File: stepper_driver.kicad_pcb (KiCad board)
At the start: 4 copper layers, 60 x 46 mm, 51 parts, among them IC1 TMC2590-TA-Trinamic, J1 BARREL_JACK, J2 Screw_Terminal_01x04, J3 CONN_01X14, J9 USB_C_Receptacle_USB2.0, Q1 Q_NPN_BEC, Q2 NCE4614, Q3 NCE4614, Q4 Q_NPN_BEC, Q5 NCE4614, Q6 NCE4614, SW1 SW_Push, U1 CH340G, U2 XC6210B332MR, U3 XL1509-5.0, U4 ESP32-WROOM-32, U6 SN74LV1T34DBV, Y1 12MHz

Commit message: Added PCB v1
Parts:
- C8: value 1uF/50V -> 1uF; footprint Capacitor_SMD:C_0603_1608Metric -> Capacitor_SMD:C_0402_1005Metric
- moved C8 0.81 mm to (138.2, 115.7)
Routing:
- net GND: track 148.5 -> 149.3 mm

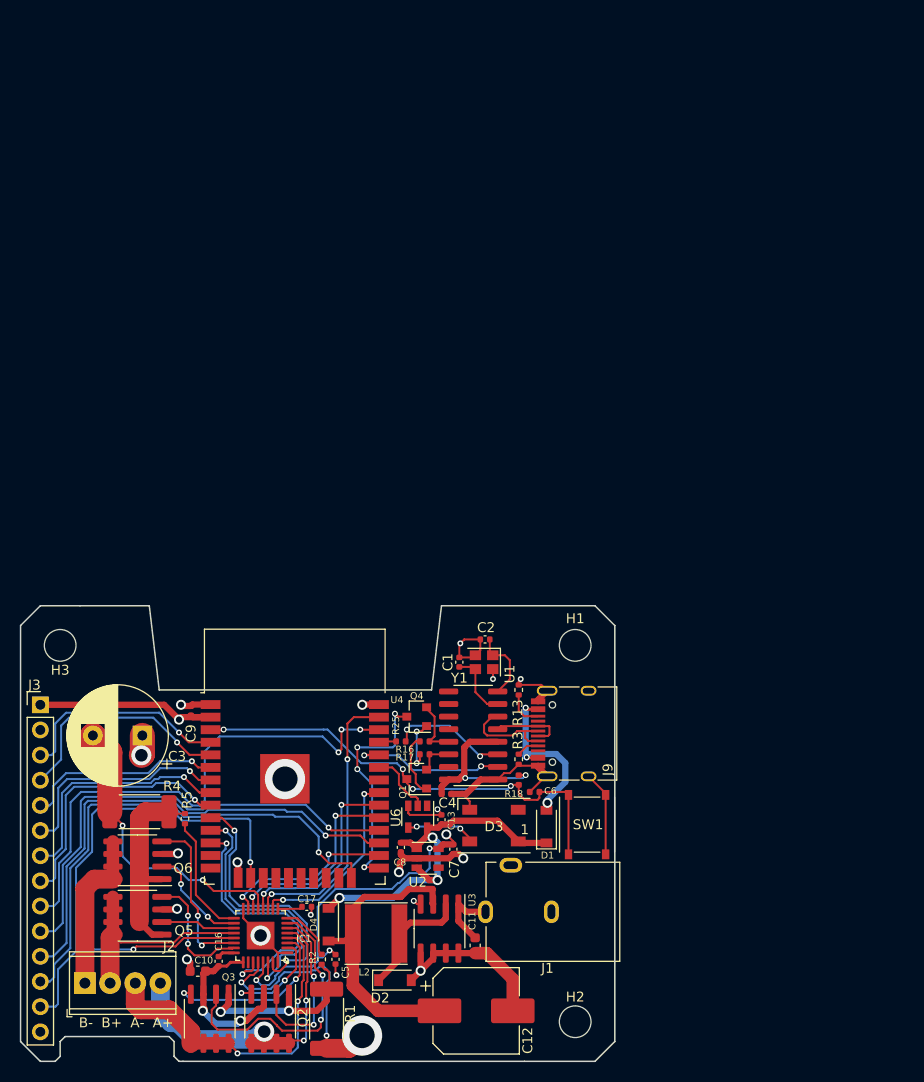
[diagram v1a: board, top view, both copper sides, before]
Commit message: Hardware design v2 with TMC2160 driver and NEMA 23 form factor for mounting
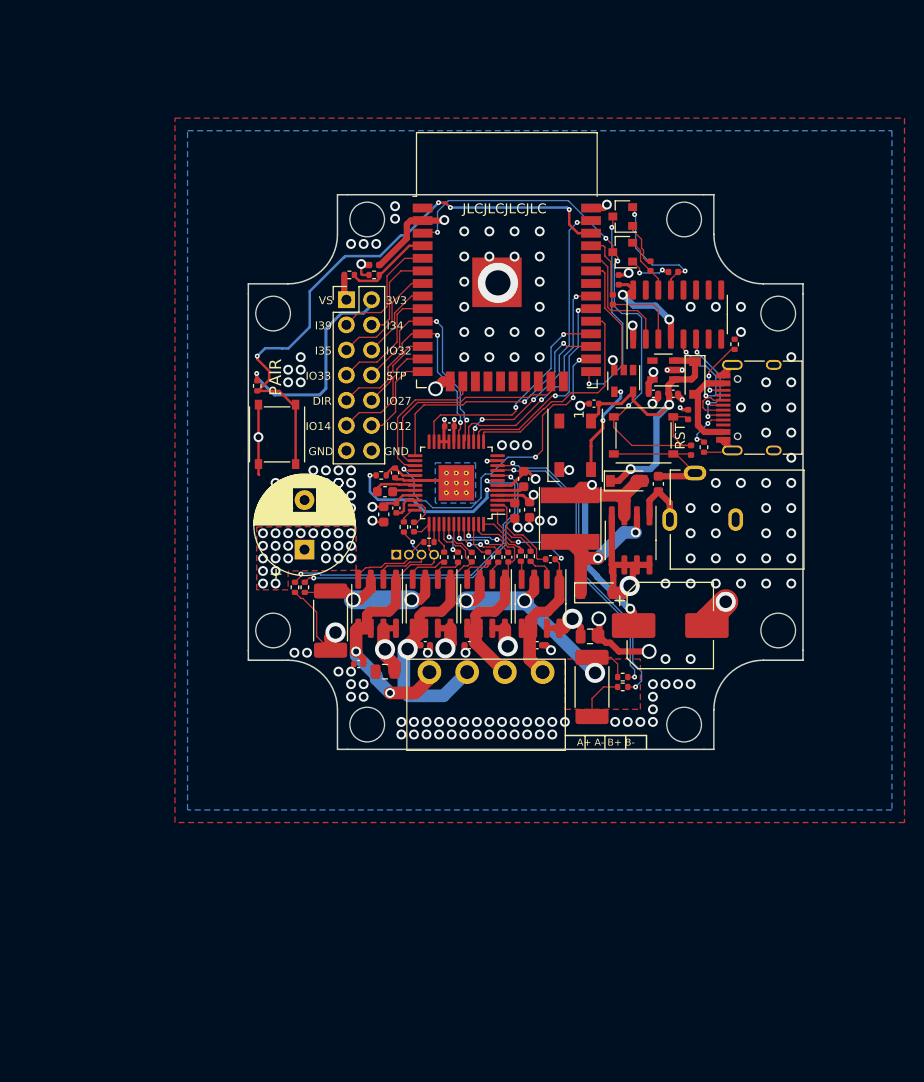
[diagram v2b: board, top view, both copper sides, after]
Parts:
- removed Y1: 12MHz, Crystal:Crystal_SMD_2520-4Pin_2.5x2.0mm
- added C14: 0.1uF, Capacitor_SMD:C_0402_1005Metric, F.Cu at (137.7, 81.4)
- added C15: 10uF/25V, Capacitor_SMD:C_0603_1608Metric, F.Cu at (149.7, 81.7)
- added C18: 10uF/25V, Capacitor_SMD:C_0603_1608Metric, F.Cu at (150.6, 78.5)
- added C19: 0.47uF/25V, Capacitor_SMD:C_0402_1005Metric, F.Cu at (137.6, 77.9)
- added C20: 0.1uF, Capacitor_SMD:C_0402_1005Metric, F.Cu at (143.1, 73.2)
- added C21: 0.1uF/50V, Capacitor_SMD:C_0603_1608Metric, F.Cu at (136.5, 82.1)
- added C22: 4.7uF/50V, Capacitor_SMD:C_0805_2012Metric, F.Cu at (136.6, 98.0)
- added C23: 4.7uF/50V, Capacitor_SMD:C_0805_2012Metric, F.Cu at (157.3, 94.4)
- added C24: 1nF/50V, Capacitor_SMD:C_0402_1005Metric, F.Cu at (152.0, 95.3)
- added C25: 1nF/50V, Capacitor_SMD:C_0402_1005Metric, F.Cu at (145.1, 95.3)
- added C26: 1nF/50V, Capacitor_SMD:C_0402_1005Metric, F.Cu at (140.7, 95.3)
- added C27: 1nF/50V, Capacitor_SMD:C_0402_1005Metric, F.Cu at (133.9, 97.2)
- added H4: MountingHole, MountingHole:MountingHole_3.5mm, F.Cu at (166.8, 103.3)
- added H5: MountingHole, MountingHole:MountingHole_3.5mm, F.Cu at (125.3, 61.8)
- added H6: MountingHole, MountingHole:MountingHole_3.5mm, F.Cu at (125.3, 93.8)
- added H7: MountingHole, MountingHole:MountingHole_3.5mm, F.Cu at (176.3, 61.8)
- added H8: MountingHole, MountingHole:MountingHole_3.5mm, F.Cu at (176.3, 93.8)
- added J4: CONN_01X04, Connector_PinHeader_1.27mm:PinHeader_1x04_P1.27mm_Vertical, B.Cu at (137.7, 86.1)
- added R10: 10R, Resistor_SMD:R_0402_1005Metric, F.Cu at (148.0, 86.4)
- added R11: 10R, Resistor_SMD:R_0402_1005Metric, F.Cu at (147.0, 86.4)
- added R12: 10R, Resistor_SMD:R_0402_1005Metric, F.Cu at (138.5, 83.3)
- added R14: 10R, Resistor_SMD:R_0402_1005Metric, F.Cu at (142.6, 86.4)
- added R15: 10R, Resistor_SMD:R_0402_1005Metric, F.Cu at (141.0, 84.9)
- added R19: 47R, Resistor_SMD:R_0402_1005Metric, F.Cu at (128.5, 89.4)
- added R20: 47R, Resistor_SMD:R_0402_1005Metric, F.Cu at (127.5, 89.4)
- added R21: 10kR, Resistor_SMD:R_0402_1005Metric, F.Cu at (133.0, 57.9)
- added R22: 470R, Resistor_SMD:R_0402_1005Metric, F.Cu at (135.5, 57.9)
- added R23: 10kR, Resistor_SMD:R_0402_1005Metric, F.Cu at (123.7, 69.1)
- added R6: 2R2, Resistor_SMD:R_0402_1005Metric, F.Cu at (136.2, 78.1)
- added R7: 10R, Resistor_SMD:R_0402_1005Metric, F.Cu at (151.3, 86.3)
- added R8: 10R, Resistor_SMD:R_0402_1005Metric, F.Cu at (150.3, 86.3)
- added R9: 47R, Resistor_SMD:R_0402_1005Metric, F.Cu at (160.6, 99.5)
- added SW2: SW_Push, Switch:SW_Push_1P1T_NO_5.1x5.1mm, F.Cu at (125.7, 74.0)
- C1: value 33pF -> 0.1uF/50V; footprint Capacitor_SMD:C_0402_1005Metric -> Capacitor_SMD:C_0603_1608Metric
- C10: value 0.1uF/50V -> 0.47uF/25V; footprint Capacitor_SMD:C_0603_1608Metric -> Capacitor_SMD:C_0402_1005Metric
- C16: value 1uF -> 0.47uF/25V
- C17: value 10uF -> 0.47uF/25V
- C2: value 33pF -> 22nF/100V; footprint Capacitor_SMD:C_0402_1005Metric -> Capacitor_SMD:C_0603_1608Metric
- C3: value 330uF/50V -> 470uF/50V
- C5: value 0.1uF -> 0.47uF/25V
- H1, H2, H3: footprint MountingHole:MountingHole_3.2mm_M3 -> MountingHole:MountingHole_3.5mm
- IC1: value TMC2590-TA-Trinamic -> TMC2160-TA; footprint TMC2590-eval:TQFP32-5x5mm -> Package_QFP:LQFP-48-1EP_7x7mm_P0.5mm_EP3.6x3.6mm_ThermalVias
- J2: footprint TerminalBlock_Phoenix:TerminalBlock_Phoenix_MPT-0,5-4-2.54_1x04_P2.54mm_Horizontal -> cixi_kefa_screw_terminals:KF2EDGR-3.81-4P
- J3: value CONN_01X14 -> CONN_02X07; footprint Connector_PinHeader_2.54mm:PinHeader_1x14_P2.54mm_Vertical -> Connector_PinHeader_2.54mm:PinHeader_2x07_P2.54mm_Vertical
- Q2, Q3, Q5, Q6: value NCE4614 -> Si4946BEY
- R2: value 10R -> 47R
- U1: value CH340G -> CH340B
- U4: value ESP32-WROOM-32 -> ESP32-WROOM-32D
- moved H2 81.7 mm to (166.8, 52.3), turned to 0 degrees
- moved Q1 57.1 mm to (160.6, 55.6)
- moved U2 54.7 mm to (164.7, 67.5), turned to 180 degrees
- moved C4 54.7 mm to (160.2, 58.4), turned to 90 degrees
- moved Q4 54.6 mm to (160.6, 52.0)
- moved U4 54.5 mm to (148.9, 59.4)
- moved R17 54.3 mm to (163.4, 57.0), turned to 270 degrees
- moved D4 54.0 mm to (161.0, 78.7), turned to 0 degrees
- moved R16 53.6 mm to (165.7, 57.6)
- moved C8 53.4 mm to (165.7, 69.9), turned to 0 degrees
- moved C10 52.3 mm to (149.0, 86.4), turned to 90 degrees
- moved J3 51.3 mm to (132.7, 60.4)
- moved J2 51.2 mm to (146.8, 98.0)
- moved Q3 50.3 mm to (146.8, 91.1)
- moved C7 50.2 mm to (163.7, 69.9), turned to 0 degrees
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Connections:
- C1 pad 1: Net-(C1-Pad1) -> VS
- C10 pad 1: VS -> /BMB2
- C10 pad 2: GND -> /CB2
- C16 pad 1: VS -> /BMA1
- C16 pad 2: Net-(C16-Pad2) -> /CA1
- C17 pad 1: Net-(C17-Pad1) -> /BMA2
- C17 pad 2: GND -> /CA2
- C2 pad 2: GND -> Net-(C2-Pad2)
- C5 pad 1: +3V3 -> /BMB1
- C5 pad 2: GND -> /CB1
- IC1 pad 1: GND -> /HB1
- IC1 pad 10: /TMC_MISO -> /SRBL
- IC1 pad 11: /TMC_MOSI -> GND
- IC1 pad 12: /TMC_CLK -> (no net)
- IC1 pad 13: GND -> /TMC_CS
- IC1 pad 14: /TMC_CS -> /TMC_CLK
- IC1 pad 15: /TMC_~EN -> /TMC_MOSI
- IC1 pad 16: GND -> /TMC_MISO
- IC1 pad 17: /SRB -> /TMC_STEP
- IC1 pad 18: /LB2 -> /TMC_DIR
- IC1 pad 19: /LB1 -> GND
- IC1 pad 2: /HA1 -> /CB1
- IC1 pad 20: /BMB1 -> +3V3
- IC1 pad 21: /BMB2 -> +3V3
- IC1 pad 22: /HB2 -> +3V3
- IC1 pad 23: /HB1 -> /TMC_DCEN
- IC1 pad 24: Net-(C16-Pad2) -> (no net)
- IC1 pad 25: VS -> /TMC_DCO
- IC1 pad 26: (no net) -> /TMC_DIAG0
- IC1 pad 27: /TMC_SG_TST -> /TMC_DIAG1
- IC1 pad 28: GND -> /TMC_~EN
- IC1 pad 29: +3V3 -> Net-(C19-Pad1)
- IC1 pad 3: /HA2 -> Net-(C15-Pad2)
- IC1 pad 30: /TMC_DIR -> GND
- IC1 pad 31: /TMC_STEP -> Net-(C2-Pad2)
- IC1 pad 32: GND -> Net-(C2-Pad1)
- IC1 pad 33: GND -> VS
- IC1 pad 4: /BMA2 -> VS
- IC1 pad 5: /BMA1 -> Net-(C18-Pad2)
- IC1 pad 6: /LA1 -> GND
- IC1 pad 7: /LA2 -> /SRAL
- IC1 pad 8: /SRA -> /SRAH
- IC1 pad 9: Net-(C17-Pad1) -> /SRBH
- J2 pad 1: /BMB2 -> /BMA2
- J2 pad 2: /BMB1 -> /BMA1
- J2 pad 3: /BMA2 -> /BMB2
- J2 pad 4: /BMA1 -> /BMB1
- J3 pad 1: +3V3 -> VS
- J3 pad 10: /IO17 -> /IO27
- J3 pad 11: /IO16 -> /IO14
- J3 pad 12: /IO2 -> /IO12
- J3 pad 13: /IO13 -> GND
- J3 pad 2: VS -> +3V3
- J3 pad 3: /I36 -> /I39
- J3 pad 4: /I39 -> /I34
- J3 pad 5: /I34 -> /I35
- J3 pad 6: /I35 -> /IO32
- J3 pad 7: /IO32 -> /IO33
- J3 pad 8: /IO33 -> /TMC_STEP
- J3 pad 9: /IO22 -> /TMC_DIR
- Q2 pad 1: Net-(Q2-Pad1) -> /BMB1
- Q2 pad 2: /LA1 -> Net-(Q2-Pad2)
- Q2 pad 3: VS -> Net-(Q2-Pad3)
- Q2 pad 4: /HA1 -> Net-(Q2-Pad4)
- Q2 pad 5: /BMA1 -> /BMB1
- Q2 pad 6: /BMA1 -> /BMB1
- Q2 pad 7: /BMA1 -> VS
- Q2 pad 8: /BMA1 -> VS
- Q3 pad 1: Net-(Q2-Pad1) -> /BMB2
- Q3 pad 2: /LA2 -> Net-(Q3-Pad2)
- Q3 pad 3: VS -> Net-(Q2-Pad3)
- Q3 pad 4: /HA2 -> Net-(Q3-Pad4)
- Q3 pad 5: /BMA2 -> /BMB2
- Q3 pad 6: /BMA2 -> /BMB2
- Q3 pad 7: /BMA2 -> VS
- Q3 pad 8: /BMA2 -> VS
- Q5 pad 1: Net-(Q5-Pad1) -> /BMA2
- Q5 pad 2: /LB1 -> /GHA2
- Q5 pad 3: VS -> Net-(Q5-Pad3)
- Q5 pad 4: /HB1 -> /GLA2
- Q5 pad 5: /BMB1 -> /BMA2
- Q5 pad 6: /BMB1 -> /BMA2
- Q5 pad 7: /BMB1 -> VS
- Q5 pad 8: /BMB1 -> VS
- Q6 pad 1: Net-(Q5-Pad1) -> /BMA1
- Q6 pad 2: /LB2 -> Net-(Q6-Pad2)
- Q6 pad 3: VS -> Net-(Q5-Pad3)
- Q6 pad 4: /HB2 -> Net-(Q6-Pad4)
- Q6 pad 5: /BMB2 -> /BMA1
- Q6 pad 6: /BMB2 -> /BMA1
- Q6 pad 7: /BMB2 -> VS
- Q6 pad 8: /BMB2 -> VS
- R1 pad 1: Net-(Q2-Pad1) -> Net-(Q2-Pad3)
- R2 pad 1: Net-(Q2-Pad1) -> Net-(Q2-Pad3)
- R2 pad 2: /SRA -> /SRBH
- R4 pad 1: Net-(Q5-Pad1) -> Net-(Q5-Pad3)
- R5 pad 1: Net-(Q5-Pad1) -> Net-(Q6-Pad2)
- R5 pad 2: /SRB -> /HA1
- U1 pad 7: Net-(C1-Pad1) -> (no net)
- U1 pad 8: Net-(C2-Pad1) -> (no net)
- U4 pad 12: /TMC_SG_TST -> /IO27
- U4 pad 13: (no net) -> /IO14
- U4 pad 14: (no net) -> /IO12
- U4 pad 16: /IO13 -> /TMC_DIAG1
- U4 pad 23: (no net) -> /TMC_DIAG0
- U4 pad 24: /IO2 -> (no net)
- U4 pad 27: /IO16 -> /TMC_DCO
- U4 pad 28: /IO17 -> /TMC_DCEN
- U4 pad 36: /IO22 -> /PAIR_SW
- U4 pad 4: /I36 -> /VS_SENSE
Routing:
- net /PAIR_SW: track 0.00 -> 59.4 mm, vias 0 -> 4
- net /IO22: track 53.3 -> 0.00 mm, vias 3 -> 0
- net /IO2: track 51.9 -> 0.00 mm, vias 1 -> 0
- net /IO16: track 49.9 -> 0.00 mm, vias 1 -> 0
- net /IO17: track 47.7 -> 0.00 mm, vias 1 -> 0
- net /IO13: track 45.1 -> 0.00 mm, vias 1 -> 0
- net GND: track 149.3 -> 106.0 mm, vias 22 -> 173
- net /SRAL: track 0.00 -> 33.5 mm, vias 0 -> 2
- net /SRBL: track 0.00 -> 32.4 mm, vias 0 -> 2
- net /SRAH: track 0.00 -> 30.9 mm, vias 0 -> 2
- net /SRBH: track 0.00 -> 30.1 mm, vias 0 -> 2
- net Net-(Q2-Pad3): track 0.00 -> 27.8 mm, vias 0 -> 3
- net /TMC_SG_TST: track 27.2 -> 0.00 mm, vias 2 -> 0
- net /LA2: track 28.2 -> 1.81 mm, vias 2 -> 0
- net /TMC_DCO: track 0.00 -> 26.2 mm, vias 0 -> 2
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- added copper zone on B.Cu, net GND
- added copper zone on F.Cu, net GND
- added copper zone on F.Cu, net VS
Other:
- board size 60 x 46 mm -> 56 x 56 mm
- net class Antenna feed: via_drill 0.35 -> 0.2
- net class Default: clearance 0.1778 -> 0.127; trace_width 0.2032 -> 0.127; via_dia 0.6 -> 0.5; via_drill 0.3 -> 0.2
- rule trace_clearance: 0.1778 -> 0.127
- rule via_min_drill: 0.3 -> 0.2
- board text added: "A+ A- B+ B-"
- board text added: "DIR"
- board text added: "Dubious Creations ESP32 Stepper Driver (Rev 2) https://github.com/matthewlai/ESP32Stepper"
- board text added: "GATE TST"
- board text added: "GH"
- board text added: "GL"
- board text added: "IO12"
- board text added: "IO14"
- board text added: "IO27"
- board text added: "JLCJLCJLCJLC"
- board text added: "MD"
- board text added: "PAIR"
- board text added: "RST"
- board text added: "STP"
- board text removed: "A+"
- board text removed: "A-"
- board text removed: "B+"
- board text removed: "B-"
- board text removed: "I36"
- board text removed: "IO13"
- board text removed: "IO16"
- board text removed: "IO17"
- board text removed: "IO2"
- board text removed: "IO22"

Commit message: Minor board updates
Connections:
- IC1 pad 12: (no net) -> GND
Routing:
- net GND: track 106.0 -> 106.5 mm

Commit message: Updated hardware to rev 3
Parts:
- removed J4: CONN_01X04, Connector_PinHeader_1.27mm:PinHeader_1x04_P1.27mm_Vertical
- removed U6: SN74LV1T34DBV, Package_TO_SOT_SMD:SOT-23-5
- added AE1: KH3216-A55, KH3216:KH3216-A55, F.Cu at (142.3, 52.2)
- added C28: 1.5pF, Capacitor_SMD:C_0603_1608Metric, F.Cu at (150.1, 53.0)
- added C30: 0.1uF, Capacitor_SMD:C_0402_1005Metric, F.Cu at (158.7, 60.8)
- added C31: 220uF/50V, Capacitor_THT:CP_Radial_D10.0mm_P5.00mm, F.Cu at (131.1, 81.9)
- added C32: 0.47uF/25V, Capacitor_SMD:C_0402_1005Metric, F.Cu at (154.5, 84.5)
- added C33: 10uF/50V, Capacitor_SMD:C_0805_2012Metric, F.Cu at (163.3, 79.7)
- added C34: 0.1uF/50V, Capacitor_SMD:C_0402_1005Metric, F.Cu at (167.2, 90.3)
- added C35: 10uF/25V, Capacitor_SMD:C_0603_1608Metric, F.Cu at (164.8, 90.1)
- added C36: 0.1uF/50V, Capacitor_SMD:C_0402_1005Metric, F.Cu at (161.8, 80.5)
- added C37: 10uF/25V, Capacitor_SMD:C_0603_1608Metric, F.Cu at (159.3, 77.8)
- added D5: 60V/1A, Diode_SMD:D_SOD-323F, F.Cu at (153.7, 82.3)
- added D6: 60V/1A, Diode_SMD:D_SOD-323F, F.Cu at (156.7, 84.2)
- added J5: Conn_Coaxial, Connector_Coaxial:U.FL_Hirose_U.FL-R-SMT-1_Vertical, F.Cu at (154.8, 52.2)
- added JP1: SolderJumper_2_Open, Resistor_SMD:R_0402_1005Metric, F.Cu at (151.8, 52.2)
- added L1: 5.1nH, Inductor_SMD:L_0603_1608Metric, F.Cu at (147.9, 52.2)
- added L3: 10uH, Inductor_SMD:L_1210_3225Metric, F.Cu at (155.4, 79.0)
- added R24: 0R, Resistor_SMD:R_0402_1005Metric, F.Cu at (151.8, 53.2)
- added R26: 10kR, Resistor_SMD:R_0402_1005Metric, F.Cu at (136.8, 76.2)
- added R27: 330kR, Resistor_SMD:R_0402_1005Metric, F.Cu at (170.7, 91.6)
- added R28: 24kR, Resistor_SMD:R_0402_1005Metric, F.Cu at (170.7, 93.5)
- added R29: 1R, Resistor_SMD:R_0402_1005Metric, F.Cu at (143.0, 86.4)
- added R30: 1R, Resistor_SMD:R_0402_1005Metric, F.Cu at (136.8, 86.5)
- added R31: 1R, Resistor_SMD:R_0402_1005Metric, F.Cu at (154.5, 86.3)
- added R32: 1R, Resistor_SMD:R_0402_1005Metric, F.Cu at (150.7, 86.3)
- added R33: 120kR, Resistor_SMD:R_0402_1005Metric, F.Cu at (160.4, 82.9)
- added R34: 22kR, Resistor_SMD:R_0402_1005Metric, F.Cu at (161.9, 82.4)
- added U5: TP6841S6-A, Package_TO_SOT_SMD:SOT-23-6, F.Cu at (159.6, 80.5)
- C11: value 1uF/50V -> 0.1uF; footprint Capacitor_SMD:C_0603_1608Metric -> Capacitor_SMD:C_0402_1005Metric
- C12: value 330uF/16V -> 10uF/50V; footprint Capacitor_SMD:CP_Elec_8x10.5 -> Capacitor_SMD:C_0805_2012Metric
- C16: value 0.47uF/25V -> 0.1uF
- C3: value 470uF/50V -> 220uF/50V
- D1: value D_Schottky -> SMBJ40A; footprint Diode_SMD:D_SOD-123 -> Diode_SMD:D_SMB
- D2, D4: value D_Schottky -> 60V/1A; footprint Diode_SMD:D_SOD-123 -> Diode_SMD:D_SOD-323F
- L2: value 68uH -> 10uH; footprint Inductor_SMD:L_Taiyo-Yuden_NR-60xx -> Inductor_SMD:L_1210_3225Metric
- U3: value XL1509-5.0 -> TP6841S6-A; footprint Package_SO:SOIC-8_3.9x4.9mm_P1.27mm -> Package_TO_SOT_SMD:SOT-23-6
- U4: value ESP32-WROOM-32D -> ESP32-PICO-D4; footprint RF_Module:ESP32-WROOM-32 -> Package_DFN_QFN:QFN-48-1EP_7x7mm_P0.5mm_EP5.3x5.3mm
- moved R23 33.8 mm to (157.4, 69.8)
- moved D1 31.8 mm to (136.2, 69.9), turned to 90 degrees
- moved SW2 29.8 mm to (155.4, 74.1), turned to 0 degrees
- moved C9 23.7 mm to (158.7, 61.8), turned to 0 degrees
- moved C6 20.2 mm to (158.2, 57.6)
- moved D2 19.5 mm to (138.8, 86.5)
- moved D4 17.6 mm to (145.1, 86.4)
- moved C11 16.5 mm to (168.2, 95.0), turned to 180 degrees
- moved R18 15.8 mm to (159.2, 58.4), turned to 270 degrees
- moved C3 14.7 mm to (131.1, 71.2), turned to 180 degrees
- moved L2 14.2 mm to (164.8, 93.2)
- moved C16 12.9 mm to (157.3, 81.5)
- moved R9 11.3 mm to (160.5, 88.2), turned to 90 degrees
- moved U3 10.5 mm to (168.3, 92.7), turned to 180 degrees
- moved R2 10.4 mm to (159.5, 88.2), turned to 90 degrees
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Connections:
- C1 pad 1: VS -> +12V
- C11 pad 1: VS -> Net-(C11-Pad1)
- C11 pad 2: GND -> Net-(C11-Pad2)
- C12 pad 1: Net-(C12-Pad1) -> VS
- C16 pad 1: /BMA1 -> Net-(C16-Pad1)
- C16 pad 2: /CA1 -> Net-(C16-Pad2)
- C24 pad 1: /BMB1 -> /BO1
- C25 pad 1: /BMB2 -> /BO2
- C26 pad 1: /BMA1 -> /AO1
- C27 pad 1: /BMA2 -> /AO2
- C5 pad 1: /BMB1 -> /BMA1
- C5 pad 2: /CB1 -> /CA1
- D1 pad 1: +5V -> VS
- D1 pad 2: Net-(D1-Pad2) -> GND
- D2 pad 1: Net-(D2-Pad1) -> /BMA2
- D3 pad 4: Net-(D3-Pad4) -> /LED_DATA
- D4 pad 1: +5V -> /BMA1
- D4 pad 2: Net-(C12-Pad1) -> GND
- IC1 pad 4: VS -> +12V
- J2 pad 1: /BMA2 -> /AO2
- J2 pad 2: /BMA1 -> /AO1
- J2 pad 3: /BMB2 -> /BO2
- J2 pad 4: /BMB1 -> /BO1
- J3 pad 10: /IO27 -> /IO32
- J3 pad 11: /IO14 -> /IO27
- J3 pad 12: /IO12 -> /IO33
- J3 pad 13: GND -> +3V3
- J3 pad 2: +3V3 -> GND
- J3 pad 3: /I39 -> /TMC_STEP
- J3 pad 4: /I34 -> /I39
- J3 pad 5: /I35 -> /TMC_DIR
- J3 pad 6: /IO32 -> /I34
- J3 pad 7: /IO33 -> /IO13
- J3 pad 8: /TMC_STEP -> /I35
- J3 pad 9: /TMC_DIR -> /IO14
- J9 pad A4: Net-(D1-Pad2) -> Net-(J9-PadA4)
- J9 pad A9: Net-(D1-Pad2) -> Net-(J9-PadA4)
- J9 pad B4: Net-(D1-Pad2) -> Net-(J9-PadA4)
- J9 pad B9: Net-(D1-Pad2) -> Net-(J9-PadA4)
- L2 pad 1: Net-(D2-Pad1) -> Net-(C11-Pad2)
- L2 pad 2: Net-(C12-Pad1) -> +12V
- Q2 pad 1: /BMB1 -> /BO1
- Q2 pad 5: /BMB1 -> /BO1
- Q2 pad 6: /BMB1 -> /BO1
- Q3 pad 1: /BMB2 -> /BO2
- Q3 pad 5: /BMB2 -> /BO2
- Q3 pad 6: /BMB2 -> /BO2
- Q5 pad 1: /BMA2 -> /AO2
- Q5 pad 5: /BMA2 -> /AO2
- Q5 pad 6: /BMA2 -> /AO2
- Q6 pad 1: /BMA1 -> /AO1
- Q6 pad 5: /BMA1 -> /AO1
- Q6 pad 6: /BMA1 -> /AO1
- U3 pad 1: VS -> Net-(C11-Pad1)
- U3 pad 2: Net-(D2-Pad1) -> GND
- U3 pad 3: Net-(C12-Pad1) -> Net-(R27-Pad2)
- U3 pad 4: GND -> VS
- U3 pad 5: GND -> VS
- U3 pad 6: GND -> Net-(C11-Pad2)
- U4 pad 1: GND -> +3V3
- U4 pad 10: /TMC_STEP -> /I34
- U4 pad 11: /TMC_DIR -> /I35
- U4 pad 12: /IO27 -> /IO32
- U4 pad 13: /IO14 -> /IO33
- U4 pad 14: /IO12 -> /TMC_STEP
- U4 pad 15: GND -> /TMC_DIR
- U4 pad 16: /TMC_DIAG1 -> /IO27
- U4 pad 17: (no net) -> /IO14
- U4 pad 19: (no net) -> +3V3
- U4 pad 2: +3V3 -> /LNA
- U4 pad 20: (no net) -> /IO13
- U4 pad 21: (no net) -> /TMC_~EN
- U4 pad 22: (no net) -> /TMC_DIAG1
- U4 pad 23: /TMC_DIAG0 -> /IO0
- U4 pad 24: (no net) -> /TMC_DIAG0
- U4 pad 25: /IO0 -> (no net)
- U4 pad 26: /TMC_~EN -> (no net)
- U4 pad 27: /TMC_DCO -> (no net)
- U4 pad 28: /TMC_DCEN -> /TMC_DCO
- U4 pad 29: /TMC_CS -> /TMC_DCEN
- U4 pad 3: /EN -> +3V3
- U4 pad 30: /TMC_CLK -> (no net)
- U4 pad 31: /TMC_MISO -> (no net)
- U4 pad 33: /LED_DATA -> (no net)
- U4 pad 34: /USB_TX -> /TMC_CS
- U4 pad 35: Net-(R25-Pad2) -> /TMC_CLK
- U4 pad 36: /PAIR_SW -> /TMC_MOSI
- U4 pad 37: /TMC_MOSI -> +3V3
- U4 pad 38: GND -> /TMC_MISO
- U4 pad 39: GND -> /PAIR_SW
- U4 pad 4: /VS_SENSE -> +3V3
- U4 pad 5: /I39 -> /VS_SENSE
- U4 pad 6: /I34 -> (no net)
- U4 pad 7: /I35 -> (no net)
- U4 pad 8: /IO32 -> /I39
- U4 pad 9: /IO33 -> /EN
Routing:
- net /PAIR_SW: track 59.4 -> 15.3 mm, vias 4 -> 2
- net +12V: track 0.00 -> 31.2 mm, vias 0 -> 2
- net Net-(C12-Pad1): track 29.6 -> 0.00 mm, vias 2 -> 0
- net /BMA1: track 33.1 -> 4.27 mm, vias 1 -> 0
- net /BMA2: track 33.9 -> 7.26 mm, vias 2 -> 0
- net /AO1: track 0.00 -> 26.4 mm, vias 0 -> 1
- net /AO2: track 0.00 -> 25.3 mm, vias 0 -> 2
- net +3V3: track 49.6 -> 24.6 mm, vias 7 -> 10
- net /EN: track 60.3 -> 38.6 mm
- net VS: track 37.1 -> 56.1 mm, vias 30 -> 31
- net /BO2: track 0.00 -> 17.3 mm
- net GND: track 106.5 -> 90.4 mm, vias 173 -> 233
- net Net-(D2-Pad1): track 15.7 -> 0.00 mm, vias 2 -> 0
- net +5V: track 31.9 -> 47.6 mm, vias 2 -> 4
- net /BO1: track 0.00 -> 15.2 mm
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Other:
- outline, holes or cut-outs redrawn
- board text added: "1"
- board text added: "13"
- board text added: "14"
- board text added: "27"
- board text added: "32"
- board text added: "33"
- board text added: "34"
- board text added: "35"
- board text added: "39"
- board text added: "Do Not Use"
- board text added: "Dubious Creations ESP32 Stepper Driver (Rev 3) GitHub: bit.ly/3KkRhnF"
- board text removed: "Dubious Creations ESP32 Stepper Driver (Rev 2) https://github.com/matthewlai/ESP32Stepper"
- board text removed: "GATE TST"
- board text removed: "GH"
- board text removed: "GL"
- board text removed: "I34"
- board text removed: "I35"
- board text removed: "I39"
- board text removed: "IO12"
- board text removed: "IO14"
- board text removed: "IO27"
- board text removed: "IO32"
- board text removed: "IO33"
- board text removed: "MD"

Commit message: Rev3 PCB tweaks
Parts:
- added C29: 2.2nF, Capacitor_SMD:C_0402_1005Metric, F.Cu at (131.0, 87.8)
- added C38: 2.2nF, Capacitor_SMD:C_0402_1005Metric, F.Cu at (160.1, 87.4)
- added C39: 0.1uF, Capacitor_SMD:C_0402_1005Metric, F.Cu at (128.1, 89.8)
- added C40: 0.1uF, Capacitor_SMD:C_0402_1005Metric, F.Cu at (159.8, 90.2)
- added H10: MountingHole, Symbol:OSHW-Logo_5.7x6mm_SilkScreen, F.Cu at (158.8, 99.3)
- added H9: MountingHole, Symbol:Symbol_Barrel_Polarity, F.Cu at (174.3, 88.8)
- added R35: 1R, Resistor_SMD:R_0402_1005Metric, F.Cu at (134.7, 81.6)
- added R36: 100kR, Resistor_SMD:R_0402_1005Metric, F.Cu at (166.2, 91.9)
- added R37: 100kR, Resistor_SMD:R_0402_1005Metric, F.Cu at (160.9, 78.1)
- C11, C16: value 0.1uF -> 0.22uF
- C21: value 0.1uF/50V -> 0.22uF/50V; footprint Capacitor_SMD:C_0603_1608Metric -> Capacitor_SMD:C_0805_2012Metric
- L2, L3: value 10uH -> 22uH
- R22: value 470R -> 150R
- moved R22 10.3 mm to (134.3, 68.1), turned to 90 degrees
- moved R21 8.71 mm to (133.7, 66.6)
- moved C37 7.03 mm to (152.3, 78.5), turned to 90 degrees
- moved L2 3.53 mm to (166.6, 96.2), turned to 180 degrees
- moved C34 3.41 mm to (165.7, 93.4), turned to 0 degrees
- moved C11 1.62 mm to (169.9, 95.0)
- moved C35 1.25 mm to (164.9, 91.3), turned to 270 degrees
- moved R19 1.02 mm to (128.6, 88.4)
- moved R20 1.02 mm to (127.6, 88.4)
- moved D1 0.96 mm to (137.1, 69.9)
- moved C12 0.90 mm to (168.5, 89.7)
- moved R6 0.71 mm to (136.2, 77.4)
- moved R9 0.61 mm to (160.5, 88.8)
- moved R2 0.61 mm to (159.5, 88.8)
- moved R27 0.38 mm to (171.0, 91.6)
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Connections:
- C14 pad 2: VS -> Net-(C14-Pad2)
- C15 pad 2: Net-(C15-Pad2) -> +12V
- C21 pad 1: VS -> Net-(C14-Pad2)
- IC1 pad 3: Net-(C15-Pad2) -> +12V
- IC1 pad 33: VS -> Net-(C14-Pad2)
- U3 pad 4: VS -> Net-(R36-Pad1)
- U5 pad 4: VS -> Net-(R37-Pad1)
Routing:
- net GND: track 90.4 -> 111.8 mm, vias 233 -> 232
- net /VS_SENSE: track 22.9 -> 32.9 mm
- net +12V: track 31.2 -> 41.0 mm
- net Net-(C14-Pad2): track 0.00 -> 5.68 mm
- net VS: track 56.1 -> 59.4 mm, vias 31 -> 27
- net +5V: track 47.6 -> 44.7 mm
- net /ANT: track 4.54 -> 1.91 mm
- net Net-(C15-Pad2): track 1.85 -> 0.00 mm
- net Net-(R37-Pad1): track 0.00 -> 1.64 mm
- net Net-(R36-Pad1): track 0.00 -> 1.50 mm
- net Net-(C40-Pad1): track 25.0 -> 26.2 mm
- net Net-(C11-Pad2): track 4.41 -> 5.40 mm
- net /SRBH: track 17.5 -> 18.4 mm
- net Net-(C39-Pad1): track 17.5 -> 18.3 mm
- net /SRBL: track 18.9 -> 19.6 mm
- added copper zone on F.Cu, net /ANT
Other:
- board text added: "+"
- board text added: "-"
- board text added: "12-36 V"
- board text added: "DO NOT USE"
- board text added: "⎓"
- board text removed: "Do Not Use"

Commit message: Cosmetics update
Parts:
- JP1: value SolderJumper_2_Open -> Open
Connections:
- net /ANT renamed Net-(C28-Pad1)
- net /CC1 renamed Net-(J9-PadA5)
- net /CC2 renamed Net-(J9-PadB5)
- net /Dm renamed Net-(J9-PadA7)
- net /Dp renamed Net-(J9-PadA6)
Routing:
- net GND: vias 232 -> 231

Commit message: Finalised rev3 files
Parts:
- removed H1: MountingHole, MountingHole:MountingHole_3.5mm
- removed L1: 5.1nH, Inductor_SMD:L_0603_1608Metric
- added R38: 0R, Resistor_SMD:R_0603_1608Metric, F.Cu at (147.4, 58.8)
- AE1: value KH3216-A55 -> IFA Antenna; footprint KH3216:KH3216-A55 -> Antennas:TI_DN007_2.4GHz
- C12, C33: footprint Capacitor_SMD:C_0805_2012Metric -> Capacitor_SMD:C_1206_3216Metric
- C28: value 1.5pF -> DNP
- D1: value SMBJ40A -> SMBJ36A
- J9: footprint Connector_USB:USB_C_Receptacle_HRO_TYPE-C-31-M-12 -> Connector_USB:USB_C_Receptacle_XKB_U262-16XN-4BVC11
- Q2, Q3, Q5, Q6: value Si4946BEY -> NCE6005AS
- R10, R11, R12, R14, R15, R5, R7, R8: value 10R -> 4.7R
- U4: footprint Package_DFN_QFN:QFN-48-1EP_7x7mm_P0.5mm_EP5.3x5.3mm -> ESP32-PICO-D4:ESP32-PICO-D4
- moved C29 23.3 mm to (151.2, 76.1), turned to 270 degrees
- moved C38 15.8 mm to (149.5, 75.7), turned to 90 degrees
- moved J5 15.4 mm to (141.1, 59.4), turned to 270 degrees
- moved AE1 12.4 mm to (154.6, 53.5)
- moved JP1 8.62 mm to (145.8, 58.4), turned to 180 degrees
- moved C28 8.23 mm to (145.2, 59.6), turned to 180 degrees
- moved R24 6.95 mm to (149.2, 59.6)
- moved R22 6.35 mm to (128.1, 66.8), turned to 0 degrees
- moved R21 5.66 mm to (128.1, 65.8)
- moved C33 5.33 mm to (161.4, 84.6), turned to 180 degrees
- moved R26 4.63 mm to (139.3, 72.3), turned to 90 degrees
- moved C6 3.83 mm to (159.3, 61.3), turned to 90 degrees
- moved R19 3.53 mm to (132.1, 88.9), turned to 0 degrees
- moved R20 3.49 mm to (124.2, 89.3), turned to 0 degrees
- moved D1 3.35 mm to (136.3, 73.2)
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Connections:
- AE1 pad 1: /ANT_OUT -> GND
- AE1 pad 2: (no net) -> /ANT_OUT
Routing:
- net GND: track 111.8 -> 123.9 mm, vias 231 -> 182
- net VS: track 59.4 -> 66.3 mm, vias 27 -> 23
- net /SRAL: track 33.9 -> 40.7 mm
- net Net-(C18-Pad2): track 20.6 -> 24.8 mm
- net +12V: track 41.0 -> 44.9 mm, vias 2 -> 4
- net Net-(Q1-Pad1): track 4.56 -> 8.37 mm
- net /SRAH: track 30.8 -> 34.6 mm
- net /TMC_STEP: track 35.0 -> 31.2 mm, vias 2 -> 3
- net /IO0: track 24.6 -> 27.8 mm
- net /TMC_MISO: track 19.8 -> 16.8 mm
- net /TMC_DIAG0: track 19.9 -> 17.0 mm
- net Net-(J5-Pad1): track 1.42 -> 4.16 mm
- net /TMC_~EN: track 23.6 -> 21.3 mm
- net /TMC_DIR: track 29.8 -> 27.5 mm
- net /SRBL: track 19.6 -> 21.8 mm
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- removed copper zone on F.Cu, net Net-(C28-Pad1)
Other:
- board text removed: "DO NOT USE"
